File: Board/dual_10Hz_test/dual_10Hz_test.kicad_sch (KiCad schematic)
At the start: 16 parts

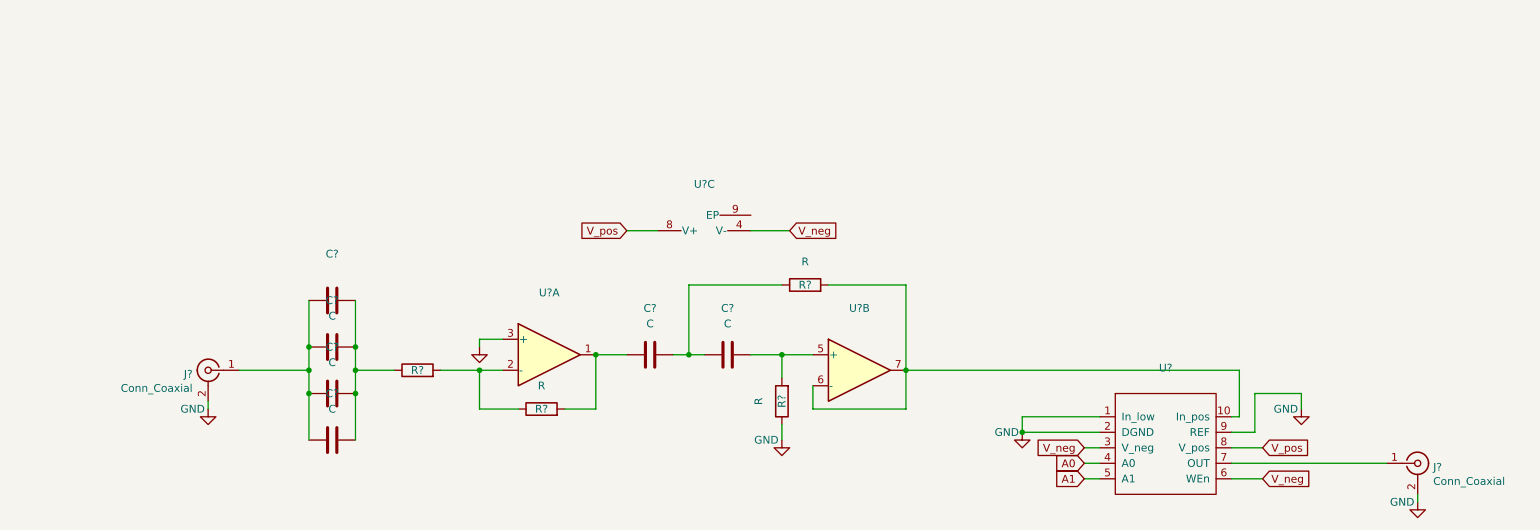
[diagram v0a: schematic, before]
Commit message: add schematic of instrumentation based approach. footprint assignment not done and layout not started
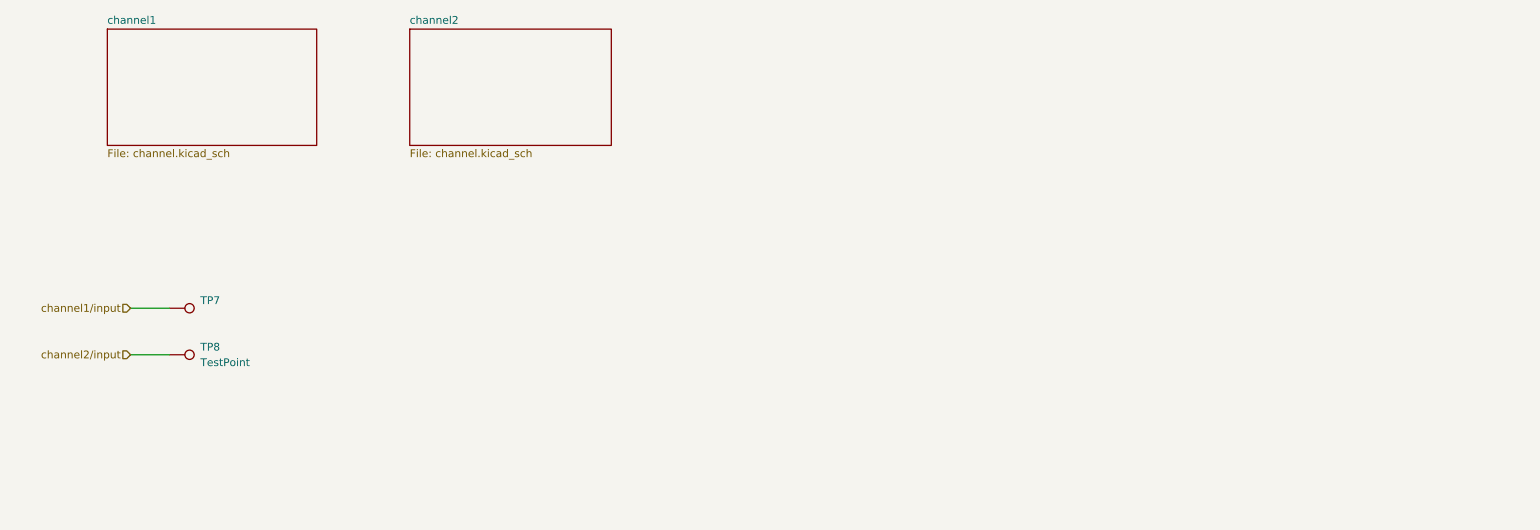
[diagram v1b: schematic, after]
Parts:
- removed C? (x5): C, symbol Device:C
- removed C?: (no value), symbol Device:C
- removed J? (x2): Conn_Coaxial, Connector_Coaxial:SMA_Molex_73251-2200_Horizontal, symbol Connector:Conn_Coaxial
- removed R? (x3): R, symbol Device:R
- removed R?: (no value), symbol Device:R
- removed U? (x3): (no value), symbol Amplifier_Operational:ADA4898-2
- removed U?: (no value), symbol SingularitySurfer_V1-rescue:AD8253-SingularitySurfer
- added TP7: (no value), symbol Connector:TestPoint
- added TP8: TestPoint, symbol Connector:TestPoint
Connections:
- new net channel1/input: TP7.1
- new net channel2/input: TP8.1
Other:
- added sheet channel1 (channel.kicad_sch)
- added sheet channel2 (channel.kicad_sch)
